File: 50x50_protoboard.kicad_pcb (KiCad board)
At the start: 2 copper layers, 50 x 50 mm, 95 parts, among them CON1 BARREL_JACK, CON2 USB-MINI-B, CON3 USB-MICRO, J1 PINS_3X1, J10 PINS_3X1, J11 PINS_3X1, J12 PINS_3X1, J13 PINS_3X1, J14 PINS_3X1, J15 PINS_3X1, J16 PINS_3X1, J17 PINS_3X1, J18 PINS_3X1, J19 PINS_3X1, J2 PINS_3X1, J20 PINS_3X1, J21 PINS_3X1, J22 PINS_3X1, J23 PINS_3X1, J24 PINS_3X1, J25 PINS_3X1, J26 PINS_3X1, J27 PINS_3X1, J28 PINS_3X1, J29 PINS_3X1, J3 PINS_3X1, J30 PINS_3X1, J31 PINS_3X1, J32 PINS_3X1, J33 PINS_3X1, J34 PINS_3X1, J35 PINS_3X1, J36 PINS_3X1, J37 PINS_3X1, J38 PINS_3X1, J39 PINS_3X1, J4 PINS_3X1, J40 PINS_3X1, J41 PINS_3X1, J42 PINS_3X1, J43 PINS_3X1, J44 PINS_3X1, J45 PINS_3X1, J46 PINS_3X1, J47 PINS_3X1, J48 PINS_3X1, J49 PINS_3X1, J5 PINS_3X1, J50 PINS_3X1, J51 PINS_3X1, J52 PINS_3X1, J53 PINS_3X1, J54 PINS_3X1, J55 PINS_3X1, J56 PINS_3X1, J57 PINS_3X1, J58 PINS_3X1, J59 PINS_3X1, J6 PINS_3X1, J60 PINS_3X1, J61 PINS_3X1, J62 PINS_3X1, J63 PINS_3X1, J64 PINS_3X1, J65 PINS_2X1, J7 PINS_3X1, J8 PINS_3X1, J9 PINS_3X1, P1 CONN_5, U1 7805

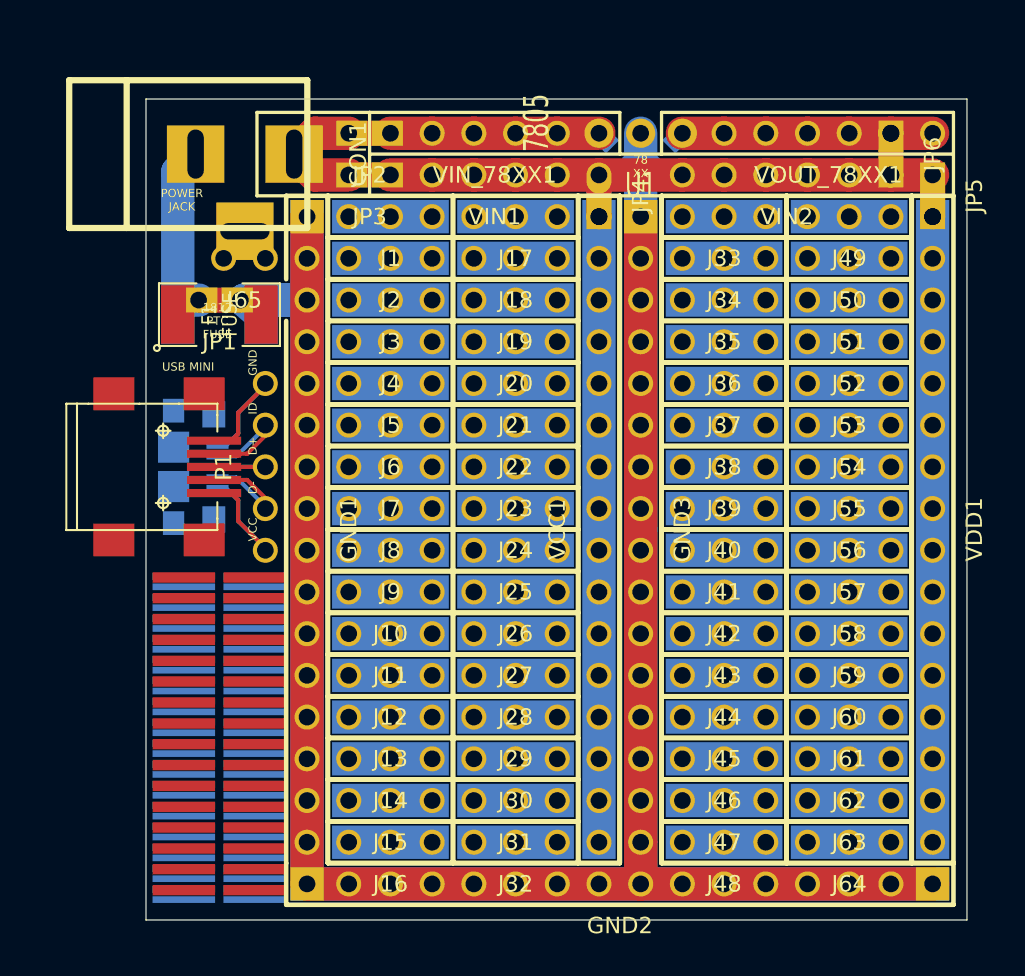
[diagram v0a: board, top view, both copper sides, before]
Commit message: switched to UNLICENSE and updated modules and directory structure to that of newer kicad projects
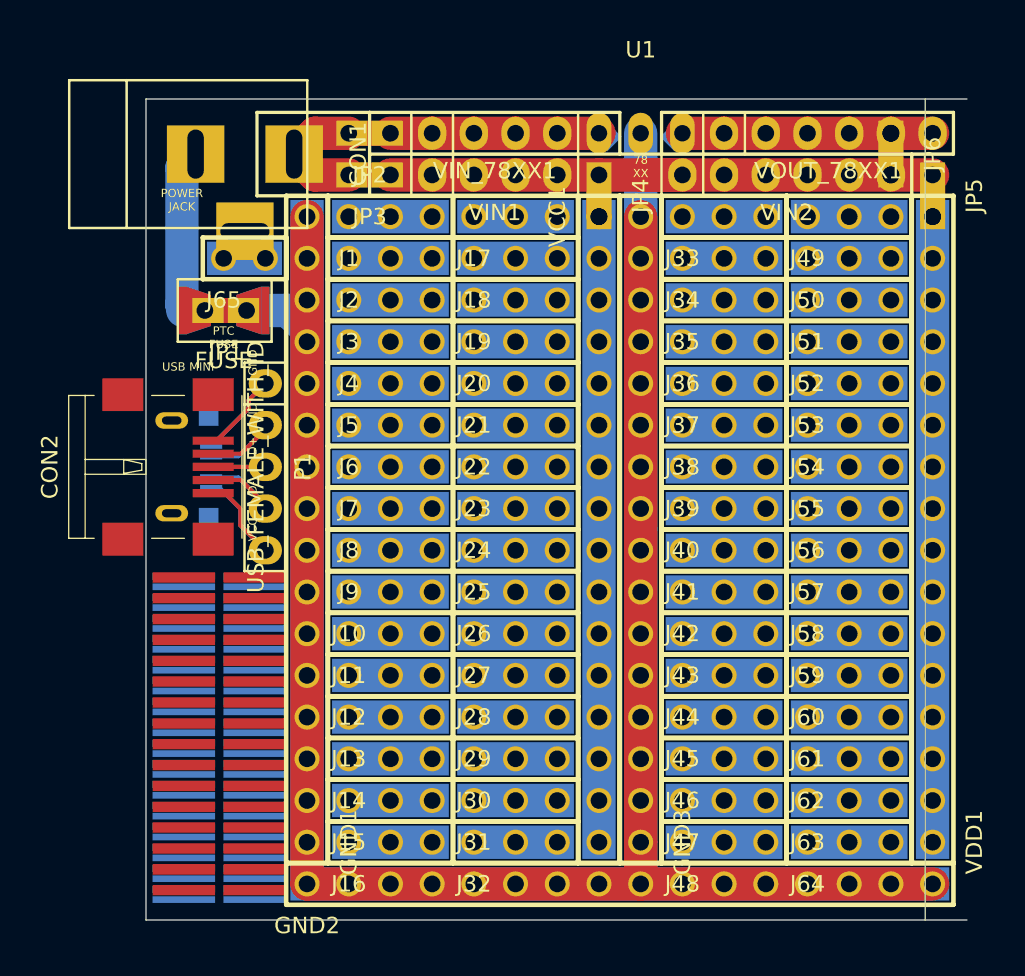
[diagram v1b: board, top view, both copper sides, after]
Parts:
- C1, C2: footprint SM0603_Capa -> Capacitors_SMD:C_0805_HandSoldering
- CON1: footprint BARREL_JACK -> Connect:BARREL_JACK
- CON2: value USB-MINI-B -> USB_FEMALE_WITH_ID; footprint CONN_USB_MINI-B -> Connectors:USB_Mini-B_Female
- CON3: value USB-MICRO -> USB_FEMALE_WITH_ID; footprint CONN_USB_MICRO-B -> Connectors:USB_Micro-B_Female_Wellco_AUSB_1011_05S2
- F1, F2: footprint SM1812L -> Muonde:CC12ZZ
- GND1, GND2, GND3, VCC1, VDD1: value PINS_16X1 -> INTERCONNECT_16X1; footprint PINS_INTERCONNECT_16X1 -> 2.54mm_Pin_Headers:Interconnect_1x16
- J1, J10, J11, J12, J13, J14, J15, J16, J17, J18, J19, J2, J20, J21, J22, J23, J24, J25, J26, J27, J28, J29, J3, J30, J31, J32, J33, J34, J35, J36, J37, J38, J39, J4, J40, J41, J42, J43, J44, J45, J46, J47, J48, J49, J5, J50, J51, J52, J53, J54, J55, J56, J57, J58, J59, J6, J60, J61, J62, J63, J64, J7, J8, J9: value PINS_3X1 -> INTERCONNECT_3X1; footprint PINS_INTERCONNECT_3X1 -> 2.54mm_Pin_Headers:Interconnect_1x03
- J65: value PINS_2X1 -> INTERCONNECT_2X1; footprint PINS_2X1 -> 2.54mm_Pin_Headers:Interconnect_1x02
- JP1, JP2, JP3, JP4, JP5, JP6: footprint PINS_RECT_2X1_SOLDER_JUMPER_SHORTED_F -> 2.54mm_Pin_Headers:Solder_Jumper_1x2_Shorted_T
- P1: footprint PINS_5X1 -> Pin_Headers:Pin_Header_Straight_1x05
- U1: value 7805 -> LM7805CT; footprint 7805_VERT -> Transistors_TO-220:TO-220_Neutral123_Vertical
- VIN1, VIN_78XX1: value PINS_4X1 -> CONN_4; footprint PINS_4X1 -> Socket_Strips:Socket_Strip_Straight_1x04
- VIN2, VOUT_78XX1: value PINS_6X1 -> CONN_6; footprint PINS_6X1 -> Socket_Strips:Socket_Strip_Straight_1x06
- moved GND1 19.1 mm to (39.4, 67.3)
- moved GND2 19.1 mm to (39.4, 69.8)
- moved GND3 19.1 mm to (59.7, 67.3)
- moved VDD1 19.1 mm to (77.5, 67.3)
- moved VCC1 19.0 mm to (57.1, 29.2)
- moved CON2 3.05 mm to (33.7, 44.5)
- moved J1 2.54 mm to (41.9, 29.2)
- moved J10 2.54 mm to (41.9, 52.1)
- moved J11 2.54 mm to (41.9, 54.6)
- moved J12 2.54 mm to (41.9, 57.1)
- moved J13 2.54 mm to (41.9, 59.7)
- moved J14 2.54 mm to (41.9, 62.2)
- moved J15 2.54 mm to (41.9, 64.8)
- moved J16 2.54 mm to (41.9, 67.3)
- moved J2 2.54 mm to (41.9, 31.8)
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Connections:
- C1 pad 1: N-0000058 -> Net-(C1-Pad1)
- C1 pad 2: N-0000083 -> Net-(C1-Pad2)
- C2 pad 1: N-0000057 -> Net-(C2-Pad1)
- C2 pad 2: N-0000083 -> Net-(C1-Pad2)
- CON1 pad 3: N-0000055 -> Net-(CON1-Pad3)
- F1 pad 2: N-0000083 -> Net-(C1-Pad2)
- F2 pad 2: N-0000083 -> Net-(C1-Pad2)
- GND1 pad 1: N-0000083 -> Net-(C1-Pad2)
- GND2 pad 1: N-0000083 -> Net-(C1-Pad2)
- GND3 pad 1: N-0000083 -> Net-(C1-Pad2)
- J65 pad 1: N-0000055 -> Net-(CON1-Pad3)
- JP1 pad 2: N-0000083 -> Net-(C1-Pad2)
- JP2 pad 2: N-0000058 -> Net-(C1-Pad1)
- JP6 pad 2: N-0000057 -> Net-(C2-Pad1)
- VIN_78XX1 pad 1: N-0000058 -> Net-(C1-Pad1)
- VIN_78XX1 pad 2: N-0000058 -> Net-(C1-Pad1)
- VIN_78XX1 pad 3: N-0000058 -> Net-(C1-Pad1)
- VIN_78XX1 pad 4: N-0000058 -> Net-(C1-Pad1)
- VOUT_78XX1 pad 1: N-0000057 -> Net-(C2-Pad1)
- VOUT_78XX1 pad 2: N-0000057 -> Net-(C2-Pad1)
- VOUT_78XX1 pad 3: N-0000057 -> Net-(C2-Pad1)
- VOUT_78XX1 pad 4: N-0000057 -> Net-(C2-Pad1)
- VOUT_78XX1 pad 5: N-0000057 -> Net-(C2-Pad1)
- VOUT_78XX1 pad 6: N-0000057 -> Net-(C2-Pad1)
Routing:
- net Net-(C1-Pad2): track 0.00 -> 253.5 mm
- net N-0000083: track 232.9 -> 0.00 mm
- net Net-(C2-Pad1): track 0.00 -> 15.2 mm
- net N-0000057: track 15.2 -> 0.00 mm
- net Net-(C1-Pad1): track 0.00 -> 12.7 mm
- net N-0000058: track 12.7 -> 0.00 mm
- net Net-(JP3-Pad2): track 33.0 -> 35.6 mm
- net Net-(CON2-Pad5): track 10.8 -> 12.4 mm
- net Net-(CON1-Pad2): track 12.4 -> 11.0 mm
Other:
- outline, holes or cut-outs redrawn
- board text added: "PTC FUSE"
- board text removed: "1812 PTC FUSE"

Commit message: added screw hole, moved fuse to VIN instead of GND and rounded the outline corners
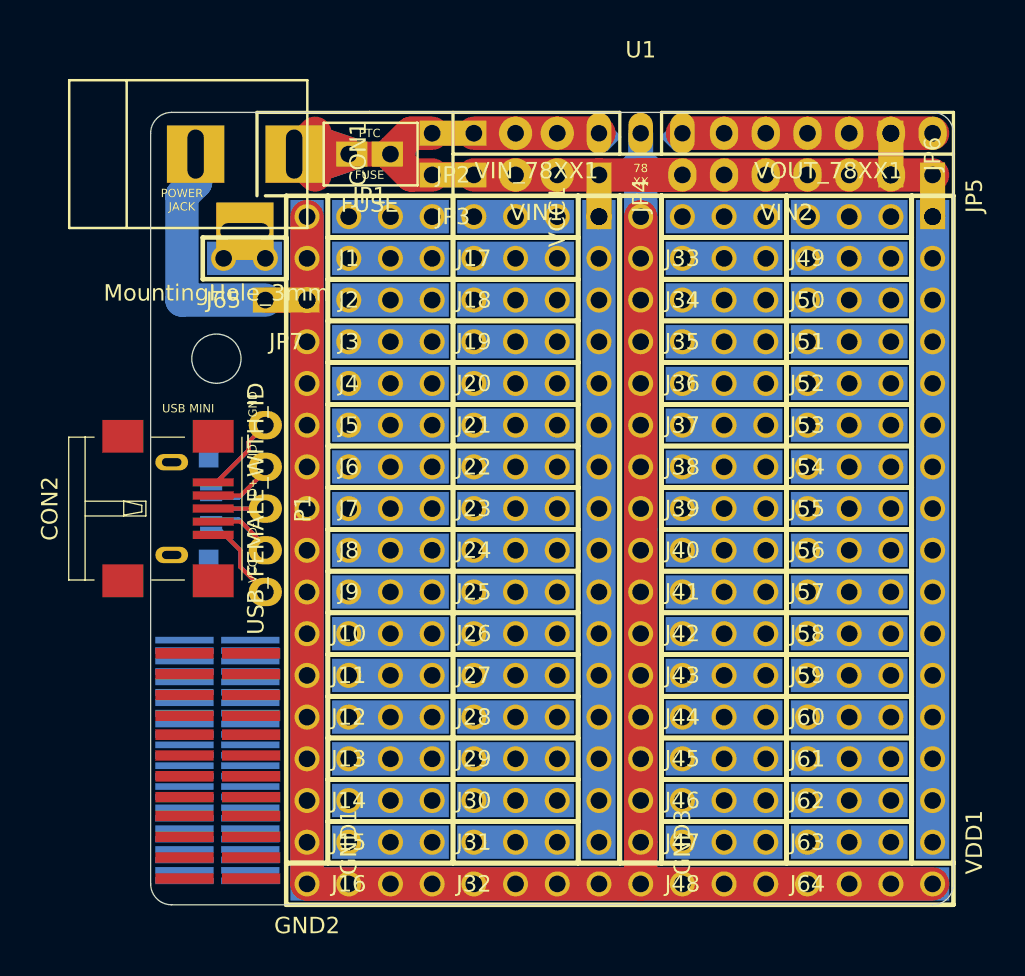
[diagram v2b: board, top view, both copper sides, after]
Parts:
- removed the Ref** at (34.0, 65.8)
- removed the Ref** at (34.0, 55.6)
- removed the Ref** at (34.0, 68.6)
- removed the Ref** at (34.0, 63.5)
- removed the Ref** at (34.0, 58.4)
- removed the Ref** at (34.0, 53.3)
- added JP7: JUMPER, 2.54mm_Pin_Headers:Solder_Jumper_1x2_Shorted_T, F.Cu at (38.1, 34.3)
- added MountingHole_3mm: VAL**, Mounting_Holes:MountingHole_3mm, F.Cu at (33.9, 37.9)
- added Ref**: Val**, SMD:SMD_065_357_8X2, B.Cu at (33.9, 57.2)
- added Ref**: Val**, SMD:SMD_065_357_8X2, B.Cu at (33.9, 62.3)
- added Ref**: Val**, SMD:SMD_065_357_8X2, B.Cu at (33.9, 67.4)
- added Ref**: Val**, SMD:SMD_127_357_4X2, F.Cu at (33.9, 67.6)
- added Ref**: Val**, SMD:SMD_127_357_4X2, F.Cu at (33.9, 62.7)
- added Ref**: Val**, SMD:SMD_127_357_4X2, F.Cu at (33.9, 57.7)
- VIN1, VIN_78XX1: value CONN_4 -> CONN_2; footprint Socket_Strips:Socket_Strip_Straight_1x04 -> Socket_Strips:Socket_Strip_Straight_1x02
- moved F1 13.0 mm to (43.2, 25.4)
- moved F2 13.0 mm to (43.2, 25.4)
- moved JP1 12.9 mm to (43.2, 25.4)
- moved JP2 5.08 mm to (48.3, 24.1)
- moved JP3 5.08 mm to (48.3, 26.7)
- moved VIN1 2.54 mm to (53.3, 26.7)
- moved VIN_78XX1 2.54 mm to (53.3, 24.1)
- moved CON2 2.54 mm to (33.7, 47.0)
- moved CON3 2.54 mm to (33.5, 47.0)
- moved P1 2.54 mm to (36.8, 47.0)
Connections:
- F1 pad 1: Net-(CON1-Pad2) -> Net-(CON1-Pad1)
- F1 pad 2: Net-(C1-Pad2) -> Net-(F1-Pad2)
- F2 pad 1: Net-(CON1-Pad2) -> Net-(CON1-Pad1)
- F2 pad 2: Net-(C1-Pad2) -> Net-(F1-Pad2)
- JP1 pad 1: Net-(CON1-Pad2) -> Net-(CON1-Pad1)
- JP1 pad 2: Net-(C1-Pad2) -> Net-(F1-Pad2)
- JP2 pad 1: Net-(CON1-Pad1) -> Net-(F1-Pad2)
- JP3 pad 1: Net-(CON1-Pad1) -> Net-(F1-Pad2)
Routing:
- net Net-(F1-Pad2): track 0.00 -> 6.13 mm
- net Net-(C1-Pad2): track 253.5 -> 248.0 mm
- net Net-(JP3-Pad2): track 35.6 -> 30.5 mm
- net Net-(C1-Pad1): track 12.7 -> 7.62 mm
- net Net-(CON1-Pad2): track 11.0 -> 14.3 mm
- net Net-(CON1-Pad1): track 7.70 -> 5.70 mm
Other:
- board size 50 x 50 mm -> 48.9 x 48.3 mm
- board text added: "FUSE"
- board text added: "PTC"
- board text removed: "PTC FUSE"
